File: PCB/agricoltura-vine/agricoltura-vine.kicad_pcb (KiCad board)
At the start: 4 copper layers, 110 x 75 mm, 96 parts, among them K1 G5LE-14_DC5, K2 G5LE-14_DC5, SW1 TL3301NF260QG, T1 BU2032SM-JJ-GTR, T10 BM04B-SRSS-TB(LF)(SN), T11 BM04B-SRSS-TB(LF)(SN), T12 BM04B-SRSS-TB(LF)(SN), T13 BM04B-SRSS-TB(LF)(SN), T14 BM04B-SRSS-TB(LF)(SN), T15 BM04B-SRSS-TB(LF)(SN), T16 0395121002, T17 0395121004, T18 0395121004, T19 TSW-108-07-G-T, T2 20021121-00010C4LF, T22 0395121006, T3 0675031020, T4 BM04B-SRSS-TB(LF)(SN), T5 BM04B-SRSS-TB(LF)(SN), T6 BM04B-SRSS-TB(LF)(SN), T7 BM04B-SRSS-TB(LF)(SN), T8 BM04B-SRSS-TB(LF)(SN), T9 BM04B-SRSS-TB(LF)(SN), U1 STM32F446RET6, U2 74HC4052D, U3 TCA9548APWR, U4 AP63203WU-7, U5 AP63205WU-7, U6 MAX13450EAUD+, U7 MAX13450EAUD+, U8 TCA6416ARTWR, X1 ABM3B-8.000MHZ-B2-T, X2 ABS07-32.768KHZ-9-T

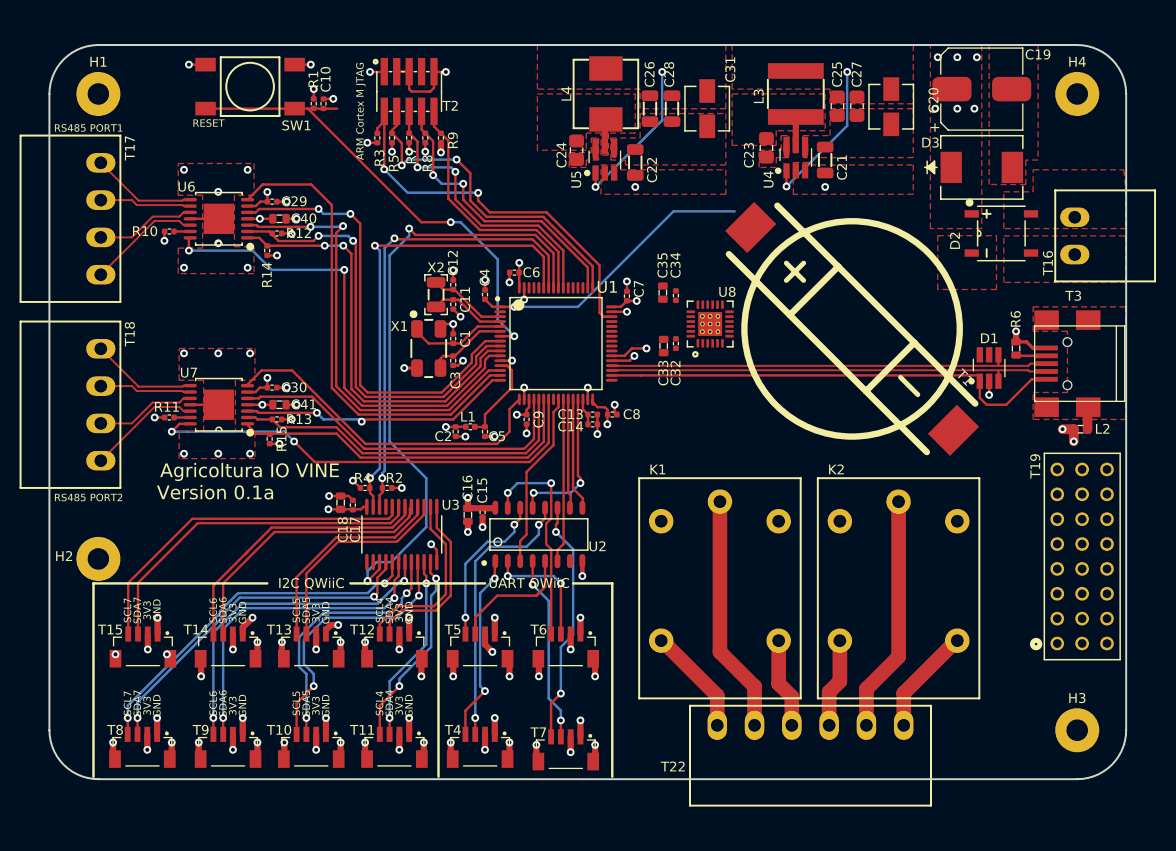
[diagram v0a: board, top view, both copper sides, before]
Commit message: Relay Driver Circuit, Board Size Change
Added the Relay driver circuitry, increased size of board tobetter acccomodate relays, figuredout the powerplane topology to get 5Vs where it needs to go.
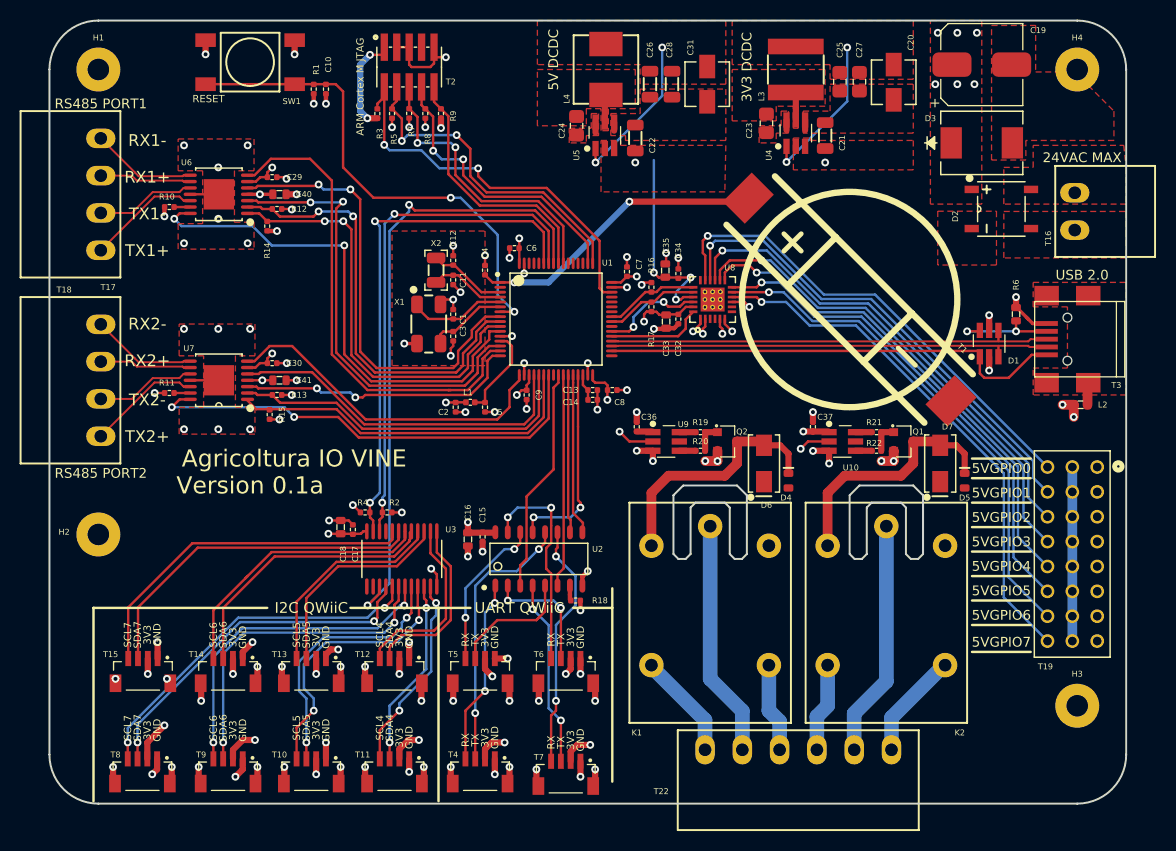
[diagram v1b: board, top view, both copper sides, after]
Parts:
- added C36: C0402C104K9PACTU, AVR-KiCAD-Lib-Resistors:R0402, F.Cu at (165.0, 101.5)
- added C37: C0402C104K9PACTU, AVR-KiCAD-Lib-Resistors:R0402, F.Cu at (183.0, 101.5)
- added D4: LTST-C194TBKT, AVR-KiCAD-Lib-Diodes:LED0603, F.Cu at (180.5, 107.0)
- added D5: LTST-C194TBKT, AVR-KiCAD-Lib-Diodes:LED0603, F.Cu at (198.5, 107.0)
- added D6: B240A-13-F, AVR-KiCAD-Lib-Diodes:B240A-13-F, F.Cu at (178.0, 105.2)
- added D7: B240A-13-F, AVR-KiCAD-Lib-Diodes:B240A-13-F, F.Cu at (196.0, 105.2)
- added Q1: IRLML6346TRPBF, AVR-KiCAD-Lib-Transistors:SOT-23, F.Cu at (192.2, 103.0)
- added Q2: IRLML6346TRPBF, AVR-KiCAD-Lib-Transistors:SOT-23, F.Cu at (174.2, 103.0)
- added R16: RC0402FR-074K7L, AVR-KiCAD-Lib-Resistors:R0402, F.Cu at (166.5, 87.2)
- added R17: RC0402FR-074K7L, AVR-KiCAD-Lib-Resistors:R0402, F.Cu at (166.5, 89.2)
- added R18: RC0402FR-071KL, AVR-KiCAD-Lib-Resistors:R0402, F.Cu at (158.8, 119.2)
- added R19: RC0402FR-0710RL, AVR-KiCAD-Lib-Resistors:R0402, F.Cu at (171.5, 102.0)
- added R20: RC0402FR-0710RL, AVR-KiCAD-Lib-Resistors:R0402, F.Cu at (171.5, 104.0)
- added R21: RC0402FR-0710RL, AVR-KiCAD-Lib-Resistors:R0402, F.Cu at (189.5, 102.0)
- added R22: RC0402FR-0710RL, AVR-KiCAD-Lib-Resistors:R0402, F.Cu at (189.5, 104.0)
- added U10: ZXGD3009E6TA, growbox-KiCAD-ICs:SOT-23-6_Handsoldering, F.Cu at (186.0, 103.0)
- added U9: ZXGD3009E6TA, growbox-KiCAD-ICs:SOT-23-6_Handsoldering, F.Cu at (168.0, 103.0)
- moved R6 3.50 mm to (203.8, 90.0)
- moved T1 3.01 mm to (186.8, 88.5)
- moved K2 2.80 mm to (190.5, 119.8)
- moved T22 2.80 mm to (181.5, 134.5)
- moved K1 2.69 mm to (172.5, 119.8)
- moved C20 2.51 mm to (191.2, 66.3)
- moved C25 2.51 mm to (185.8, 66.2)
- moved C27 2.51 mm to (187.8, 66.2)
- moved C32 2.51 mm to (169.2, 90.5)
- moved C33 2.51 mm to (168.0, 90.8)
- moved U8 2.51 mm to (172.8, 88.5)
- moved C1 2.50 mm to (146.2, 90.0)
- moved C11 2.50 mm to (146.2, 86.5)
- moved C12 2.50 mm to (146.2, 84.5)
- moved C13 2.50 mm to (160.5, 97.8)
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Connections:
- C11 pad 2: /STM32F446RET Controller/OSC32_OUT -> Net-(C11-Pad2)
- K1 pad 2: Net-(K1-Pad2) -> +5V
- K2 pad 2: Net-(K2-Pad2) -> +5V
- T19 pad 1: Net-(T19-Pad1) -> GND
- T19 pad 10: Net-(T19-Pad10) -> GND
- T19 pad 12: GND -> Net-(T19-Pad12)
- T19 pad 13: Net-(T19-Pad13) -> GND
- T19 pad 15: GND -> Net-(T19-Pad15)
- T19 pad 16: Net-(T19-Pad16) -> GND
- T19 pad 18: GND -> Net-(T19-Pad18)
- T19 pad 19: Net-(T19-Pad19) -> GND
- T19 pad 21: GND -> Net-(T19-Pad21)
- T19 pad 22: Net-(T19-Pad22) -> GND
- T19 pad 24: GND -> Net-(T19-Pad24)
- T19 pad 3: GND -> Net-(T19-Pad3)
- T19 pad 4: Net-(T19-Pad4) -> GND
- T19 pad 6: GND -> Net-(T19-Pad6)
- T19 pad 7: Net-(T19-Pad7) -> GND
- T19 pad 9: GND -> Net-(T19-Pad9)
- U1 pad 37: /STM32F446RET Controller/5VGPIO_BD_7 -> /5V IO Interfaces/IO_RESET
- U1 pad 38: Net-(U1-Pad38) -> /5V IO Interfaces/IO_INT_N
- U1 pad 40: Net-(U1-Pad40) -> /5V IO Interfaces/IO_SDA
- U1 pad 41: Net-(U1-Pad41) -> /5V IO Interfaces/IO_SCL
- U8 pad 10: Net-(T19-Pad1) -> Net-(T19-Pad24)
- U8 pad 11: Net-(T19-Pad4) -> Net-(T19-Pad21)
- U8 pad 12: Net-(T19-Pad7) -> Net-(T19-Pad18)
- U8 pad 13: Net-(T19-Pad10) -> Net-(T19-Pad15)
- U8 pad 14: Net-(T19-Pad13) -> Net-(T19-Pad12)
- U8 pad 15: Net-(T19-Pad16) -> Net-(T19-Pad9)
- U8 pad 16: Net-(T19-Pad19) -> Net-(T19-Pad6)
- U8 pad 17: Net-(T19-Pad22) -> Net-(T19-Pad3)
- U8 pad 25: Net-(U8-Pad25) -> GND
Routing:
- net Earth: track 101.0 -> 222.6 mm
- net Net-(T19-Pad24): track 0.00 -> 54.2 mm, vias 0 -> 1
- net Net-(T19-Pad21): track 0.00 -> 52.3 mm, vias 0 -> 1
- net Net-(T19-Pad15): track 0.00 -> 51.0 mm, vias 0 -> 1
- net Net-(T19-Pad18): track 0.00 -> 50.8 mm, vias 0 -> 1
- net Net-(T19-Pad12): track 0.00 -> 49.9 mm, vias 0 -> 1
- net Net-(T19-Pad9): track 0.00 -> 49.8 mm, vias 0 -> 1
- net Net-(T19-Pad6): track 0.00 -> 49.8 mm, vias 0 -> 1
- net Net-(T19-Pad3): track 0.00 -> 49.3 mm, vias 0 -> 1
- net +5V: track 21.0 -> 63.4 mm, vias 4 -> 8
- net +3V3: track 77.5 -> 103.4 mm, vias 36 -> 39
- net Net-(D5-Pad2): track 0.00 -> 25.6 mm
- net Net-(D4-Pad2): track 0.00 -> 25.4 mm
- net GND: track 127.7 -> 149.0 mm, vias 85 -> 100
- net /5V IO Interfaces/IO_INT_N: track 0.00 -> 10.6 mm, vias 0 -> 2
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- added copper zone on In2.Cu, net +5V
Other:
- board size 110 x 75 mm -> 110 x 80 mm
- board text added: "24VAC MAX"
- board text added: "3V3 DCDC"
- board text added: "5V DCDC"
- board text added: "5VGPIO0"
- board text added: "5VGPIO1"
- board text added: "5VGPIO2"
- board text added: "5VGPIO3"
- board text added: "5VGPIO4"
- board text added: "5VGPIO5"
- board text added: "5VGPIO6"
- board text added: "5VGPIO7"
- board text added: "RX"
- board text added: "RX1+"
- board text added: "RX1-"
- board text added: "RX2+"
- board text added: "RX2-"
- board text added: "TX"
- board text added: "TX1+"
- board text added: "TX1-"
- board text added: "TX2+"
- board text added: "TX2-"
- board text added: "USB 2.0"

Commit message: First pass of board
Finished routing first pass of PCB
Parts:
- moved C10 2.26 mm to (133.0, 69.2)
- moved R1 2.26 mm to (131.8, 69.2)
- moved SW1 2.26 mm to (125.2, 66.5)
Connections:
- U8 pad 1: Net-(U8-Pad1) -> /5V IO Interfaces/DRV1
- U8 pad 6: Net-(U8-Pad6) -> /5V IO Interfaces/DRV2
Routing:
- net +5V: track 63.4 -> 120.6 mm, vias 8 -> 13
- net /5V IO Interfaces/DRV2: track 3.21 -> 22.0 mm, vias 1 -> 2
- net /5V IO Interfaces/DRV1: track 3.81 -> 21.5 mm, vias 1 -> 2
- net +3V3: track 103.4 -> 111.7 mm, vias 39 -> 43
- net GND: track 149.0 -> 155.7 mm, vias 100 -> 120
- net /STM32F446RET Controller/NRST: track 50.8 -> 48.6 mm
- net Net-(U8-Pad6): track 1.59 -> 0.00 mm, vias 1 -> 0
- net Net-(U8-Pad1): track 1.59 -> 0.00 mm, vias 1 -> 0
- net Net-(T19-Pad15): track 51.0 -> 49.8 mm
- net +24V: vias 8 -> 16
